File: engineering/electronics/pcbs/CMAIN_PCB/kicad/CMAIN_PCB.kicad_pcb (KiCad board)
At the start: 4 copper layers, 210.2 x 220 mm, 258 parts, among them IC1 TSYS01, J1 RPI_5_WITH_SSQ-120-01-F-D, J10 1778719, J11 M9N-G4-3100, J12 B04B-JWPF-SK-R, J13 B04B-JWPF-SK-R, J14 XT30PW-F, J15 SM04B-GHS-TB_LF__SN_, J16 1778719, J17 SM03B-GHS-TB(LF)(SN), J19 1778719, J2 1778719, J21 1778719, J23 B04B-JWPF-SK-R, J24 1778719, J25 B08B-JWPF-SK-R, J26 B08B-JWPF-SK-R, J27 B04B-JWPF-SK-R, J28 B08B-JWPF-SK-R, J29 B06B-JWPF-SK-R, J3 AXK6S00547YG, J30 B06B-JWPF-SK-R, J31 B06B-JWPF-SK-R, J32 B04B-JWPF-SK-R, J34 B08B-JWPF-SK-R, J35 SM04B-GHS-TB_LF__SN_, J36 SM05B-GHS-TB_LF__SN_, J37 B04B-JWPF-SK-R, J38 B04B-JWPF-SK-R, J39 B04B-JWPF-SK-R, J4 AXK6S00547YG, J40 B04B-JWPF-SK-R, J41 SM06B-GHS-TB_LF__SN_, J42 B08B-JWPF-SK-R, J43 B04B-JWPF-SK-R, J44 B08B-JWPF-SK-R, J45 B04B-JWPF-SK-R, J46 B04B-JWPF-SK-R, J47 GIGABLOX_NANO_SWITCH_REVA_MOD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, J48 B04B-JWPF-SK-R, J49 B04B-JWPF-SK-R, J5 SM04B-GHS-TB_LF__SN_, J50 1814935, J51 GIGABLOX_NANO_SWITCH_REVA_MOD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, J52 B04B-JWPF-SK-R, J53 B04B-JWPF-SK-R, J55 B04B-JWPF-SK-R, J56 B04B-JWPF-SK-R, J57 B04B-JWPF-SK-R, J6 1778719, J7 SM04B-GHS-TB_LF__SN_, J8 B04B-JWPF-SK-R, J9 SM04B-GHS-TB_LF__SN_, K1 CPC1019N, K10 CPC1019N, K2 CPC1019N, K4 CPC1019N, K5 CPC1019N, K6 CPC1019N, K7 CPC1019N, K8 CPC1019N, K9 CPC1019N, Q1 SIRA99DP-T1-GE3, Q2 SIRA99DP-T1-GE3, Q4 PSMN4R3-30BL,118, Q5 PSMN4R3-30BL,118, Q6 PSMN4R3-30BL,118, Q7 PSMN4R3-30BL,118, Q8 PSMN4R3-30BL,118, Q9 PSMN4R3-30BL,118, U1 TJA1049T/3J, U10 SMTSO25100CTJ, U11 SMTSO25100CTJ, U12 SMTSO25100CTJ, U13 SMTWEM245STR, U14 SMTWEM245STR, U15 SMTWEM245STR, U16 SMTWEM245STR, U17 SY8205FCC, U18 SY8205FCC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

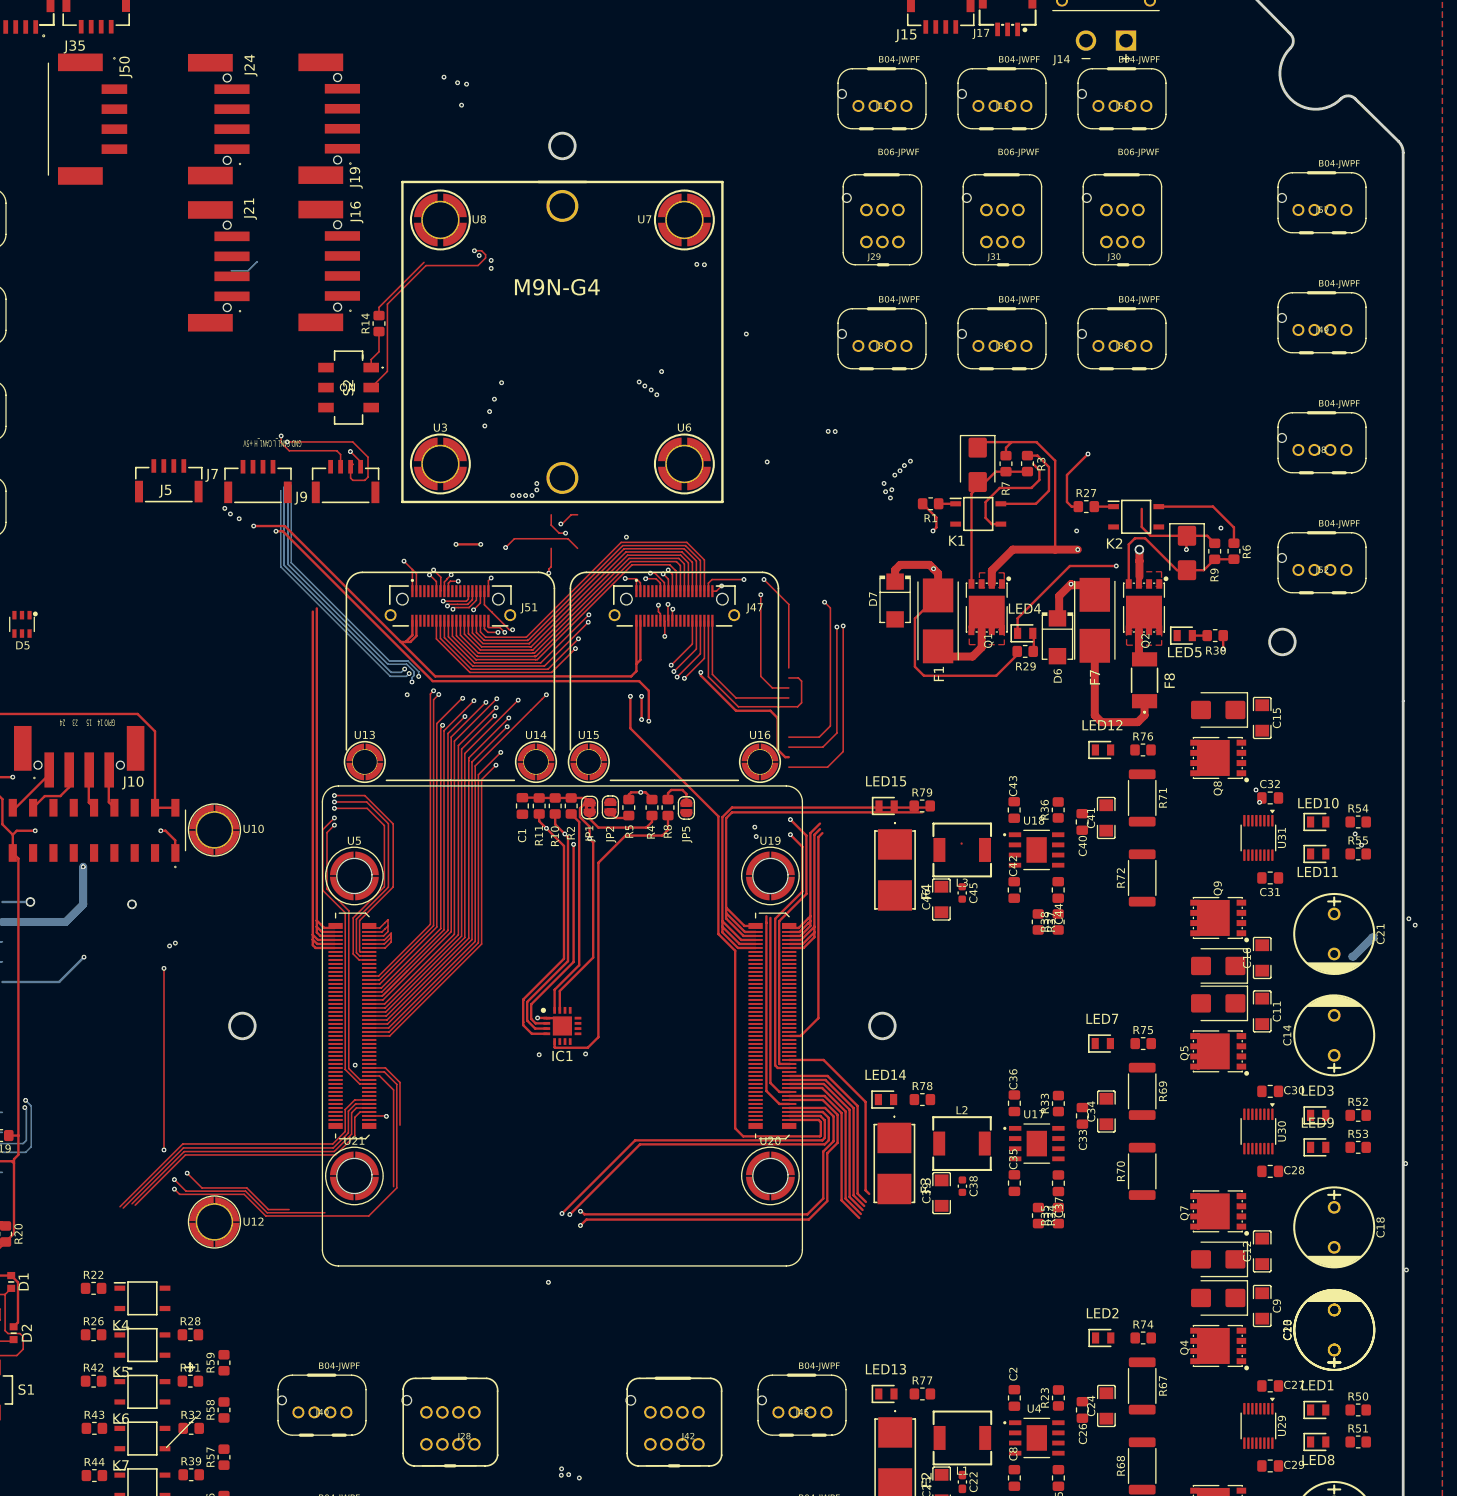
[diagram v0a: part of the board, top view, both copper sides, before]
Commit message: electronics: integrate CMAIN STEP updates and consolidate footprints
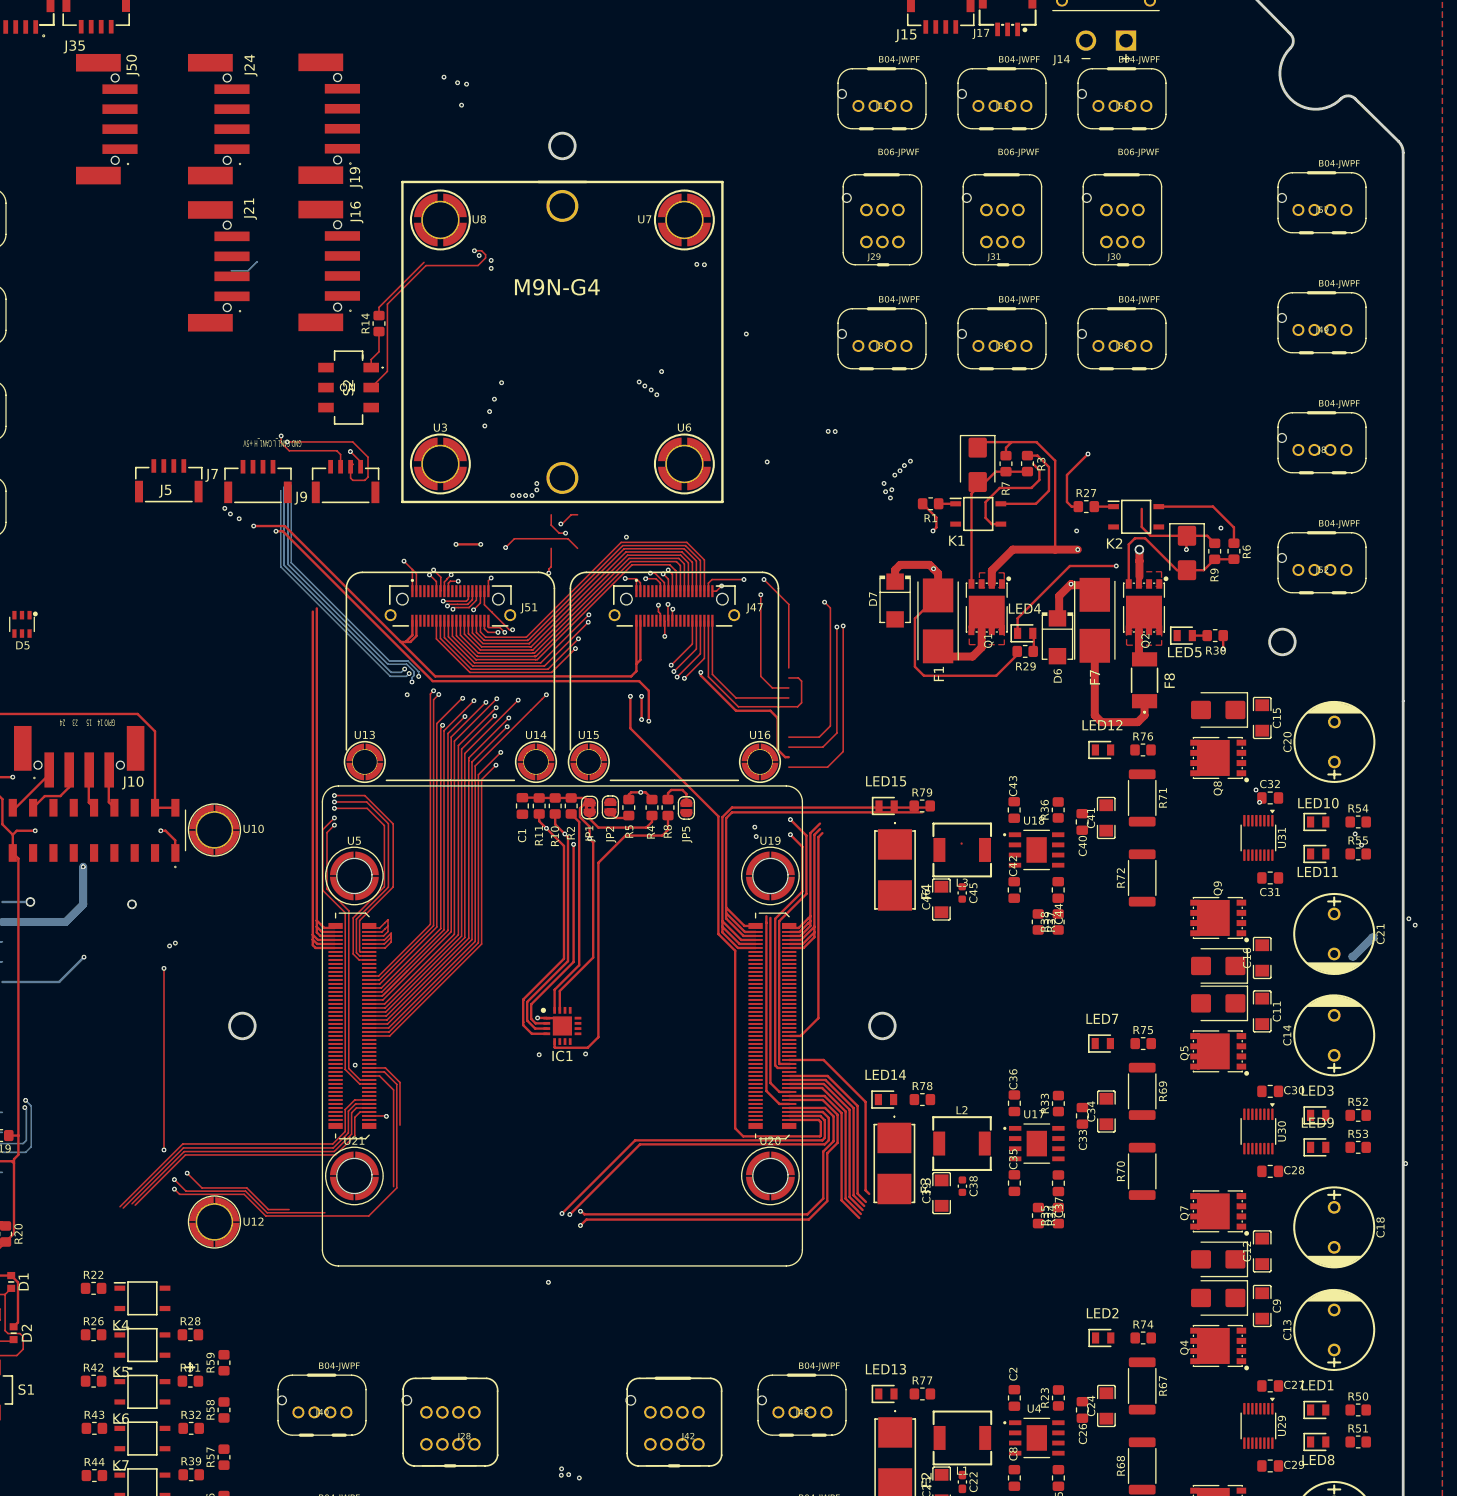
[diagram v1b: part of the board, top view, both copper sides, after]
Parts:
- CN18, CN20, CN22, CN54: footprint EasyEDA_Lib_CMAIN:CONN-SMD_4P-P1.25_BM04B-GHS-TBT-LF-SN -> EasyEDA_Lib:fp_49628edcd6
- D5: footprint EasyEDA_Lib_CMAIN:SOT-23-6_L2.9-W1.6-P0.95-LS2.8-BL -> EasyEDA_Lib:SOT-23-6_L2.9-W1.6-P0.95-LS2.8-BL
- D8: footprint EasyEDA_Lib_CMAIN:SMA_L4.3-W2.6-LS5.0-FD -> EasyEDA_Lib:SMA_L4.3-W2.6-LS5.0-FD
- F2, F3, F4: footprint Samacsys:0154005DR -> CMAIN_PCB:0154005DR
- IC1: footprint Samacsys:QFN65P400X400X90-17N -> CMAIN_PCB:QFN65P400X400X90-17N
- J1: footprint Samacsys:SSM-120-XXX-DV -> CMAIN_PCB:SSM-120-XXX-DV
- J10, J16, J19, J2, J21, J24, J6: footprint Samacsys:1778719 -> CMAIN_PCB:1778719
- J11: footprint Samacsys_kicad_sym:M9N-G4-3100 -> CMAIN_PCB:M9N-G4-3100
- J47, J51: footprint Snapeda:fp_072ec239da -> CMAIN_PCB:fp_072ec239da
- J50: value 1814935 -> 1778719; footprint CMAIN_PCB:1814935 -> CMAIN_PCB:1778719
- L1, L2, L3: footprint EasyEDA_Lib_CMAIN:IND-SMD_CYA0650-3.3UH -> EasyEDA_Lib:IND-SMD_CYA0650-3.3UH
- S1, S2: footprint Samacsys:SLW9135352ASMT -> CMAIN_PCB:SLW9135352ASMT
- U1: footprint Samacsys:SOIC127P600X175-8N -> CMAIN_PCB:SOIC127P600X175-8N
- U10, U11, U12, U9: footprint Snapeda:SMD_BD5.6-L5.6-W5.6-D4.1 -> CMAIN_PCB:SMD_BD5.6-L5.6-W5.6-D4.1
- U13, U14, U15, U16: footprint Snapeda:SCREW-SMD_BD4.4-D2.8-H4.5 -> CMAIN_PCB:SCREW-SMD_BD4.4-D2.8-H4.5
- U19, U20, U21, U5: footprint EasyEDA_Lib_CMAIN:SMD_SMTSO3060CTJ -> EasyEDA_Lib:SMD_SMTSO3060CTJ
- U2: footprint Samacsys:SOIC127P1030X265-18N -> CMAIN_PCB:SOIC127P1030X265-18N
- U3, U6, U7, U8: footprint Snapeda:SMD_BD6.0-D4.2 -> CMAIN_PCB:SMD_BD6.0-D4.2
- USB33: footprint EasyEDA_Lib_CMAIN:USB-C-SMD_TYPEC-303-ACP16 -> EasyEDA_Lib:USB-C-SMD_TYPEC-303-ACP16
- moved C20 73.5 mm to (296.5, 114.5)
- moved J50 2.00 mm to (142.0, 36.6), turned to 90 degrees
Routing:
- net GND: vias 28 -> 27
